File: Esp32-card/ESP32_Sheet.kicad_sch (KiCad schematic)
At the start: 1 part

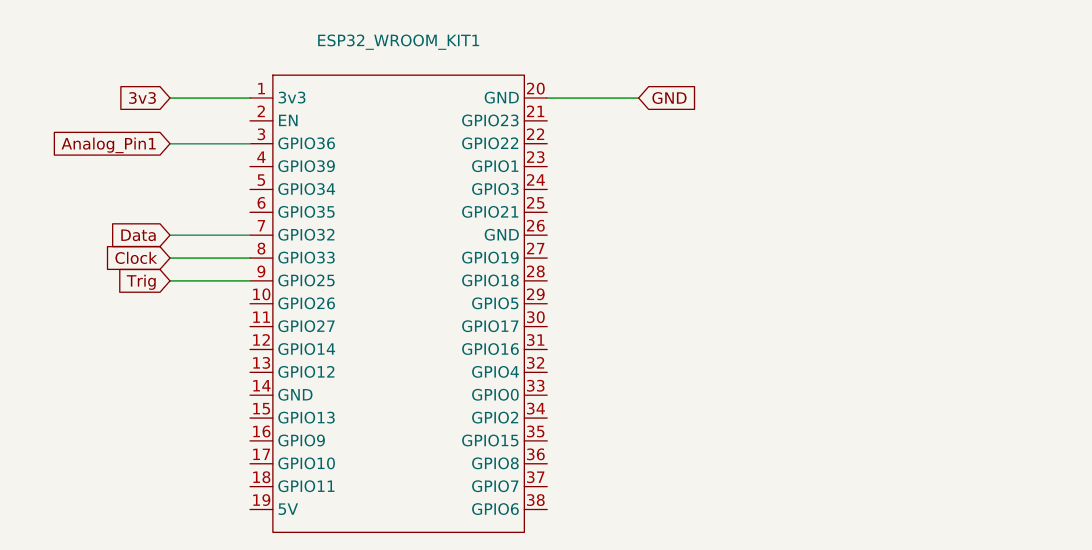
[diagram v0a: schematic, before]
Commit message: Esp32 Lib avec fichier 3d
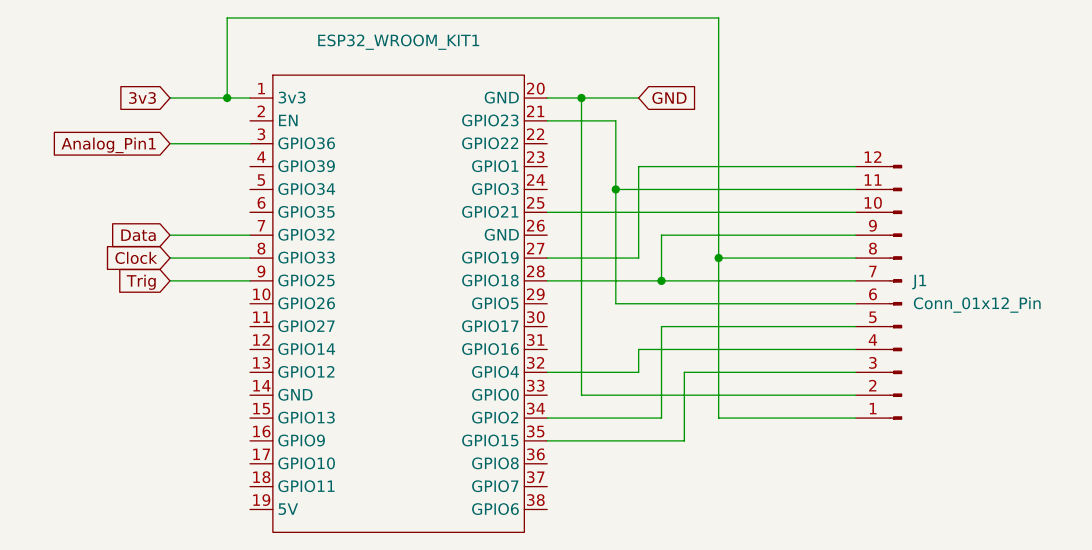
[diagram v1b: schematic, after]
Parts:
- added J1: Conn_01x12_Pin, Connector_PinHeader_2.54mm:PinHeader_1x12_P2.54mm_Horizontal, symbol Connector:Conn_01x12_Pin
- ESP32_WROOM_KIT1: footprint (none) -> MyEsp32Library:Esp32_Wroom32_DevKit
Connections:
- net 3v3: now also J1.1 (Pin_1), J1.8 (Pin_8)
- net GND: now also J1.2 (Pin_2)
- net at ESP32_WROOM_KIT1.21 (GPIO23): now also J1.11 (Pin_11), J1.6 (Pin_6)
- net at ESP32_WROOM_KIT1.25 (GPIO21): now also J1.10 (Pin_10)
- net at ESP32_WROOM_KIT1.27 (GPIO19): now also J1.12 (Pin_12)
- net at ESP32_WROOM_KIT1.28 (GPIO18): now also J1.7 (Pin_7), J1.9 (Pin_9)
- net at ESP32_WROOM_KIT1.32 (GPIO4): now also J1.4 (Pin_4)
- net at ESP32_WROOM_KIT1.34 (GPIO2): now also J1.5 (Pin_5)
- net at ESP32_WROOM_KIT1.35 (GPIO15): now also J1.3 (Pin_3)

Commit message: Alimentation
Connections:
- net 5v: now reaches ESP32_WROOM_KIT1.19 (5V)
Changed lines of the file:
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@@
+	(wire
+		(pts
+			(xy 120.65 113.03) (xy 129.54 113.03)
+		)
+		(stroke
+			(width 0)
+			(type default)
+		)
+	)
 	(wire
 		(pts
@@
 			(effects
 				(font
+					(size 1.27 1.27)
+				)
+				(justify right)
+				(hide yes)
+			)
+		)
+	)
+	(global_label "5v"
+		(shape input)
+		(at 120.65 113.03 180)
+		(fields_autoplaced yes)
+		(effects
+			(font
+				(size 1.27 1.27)
+			)
+			(justify right)
+		)
+		(property "Intersheetrefs" "${INTERSHEET_REFS}"
+			(at 115.4877 113.03 0)
+			(effects
+				(font
